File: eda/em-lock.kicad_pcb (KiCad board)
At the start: 2 copper layers, 55.9 x 55.9 mm, 81 parts, among them CON1 BARREL_JACK, P1 EXT_LED_CONN, P10 BOOT_SEL_CONN, P12 SWD_CONN, P2 RC522A, P3 RC522B, P4 BTN_OPEN, P5 BTN_CALL, P6 ESP8266_CONN, P7 LOCK_CONN, P8 PWR_SELECT, P9 PWR_SW_CONN, Q1 MMBT3906, Q2 MMBT3906, Q3 MMBT3906, Q4 Q_NMOS_DGS, SW1 RST_BTN, U1 74LVC2G14, U2 LD1117S33CTR, U3 STM32F103C8Tx, Y1 8MHz

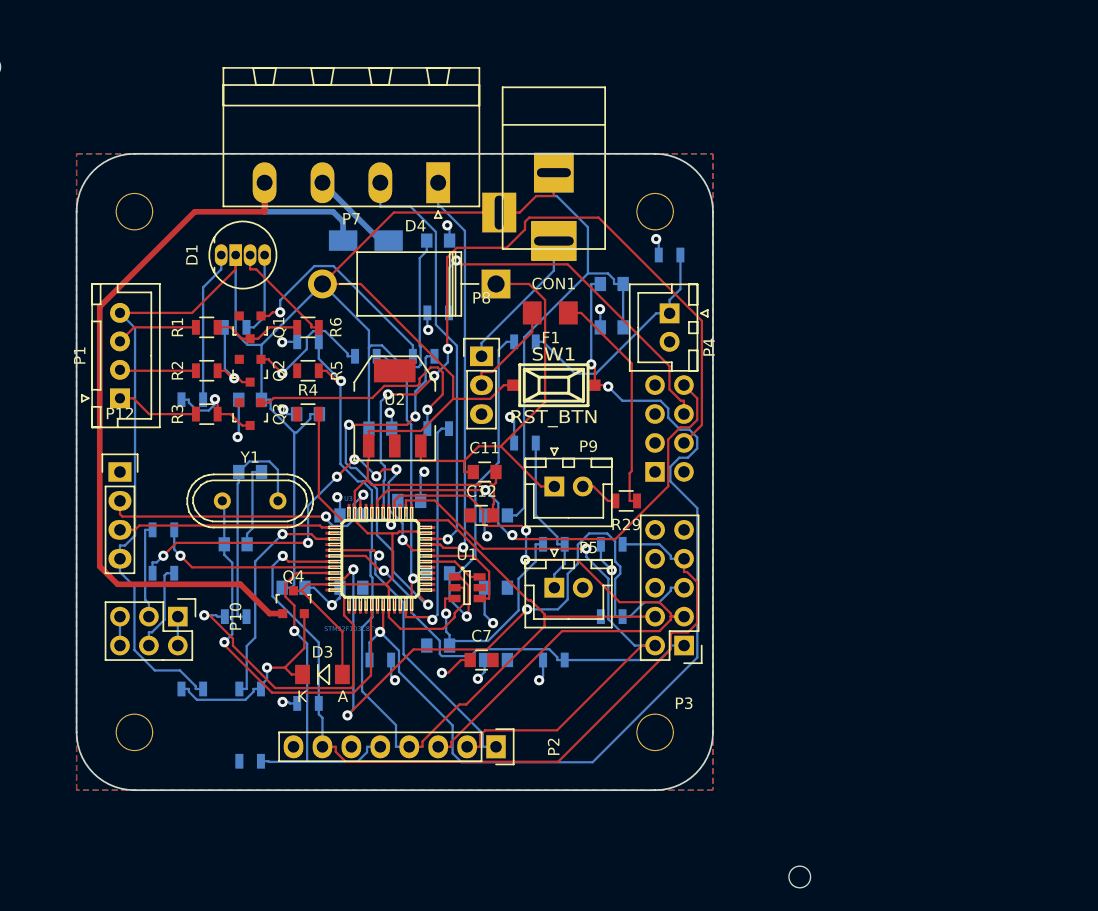
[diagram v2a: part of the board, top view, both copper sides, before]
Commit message: refs #41563 rc522 moved up, RGB LEDs moved to separate pcbs, 3d model of rc522 implemented.
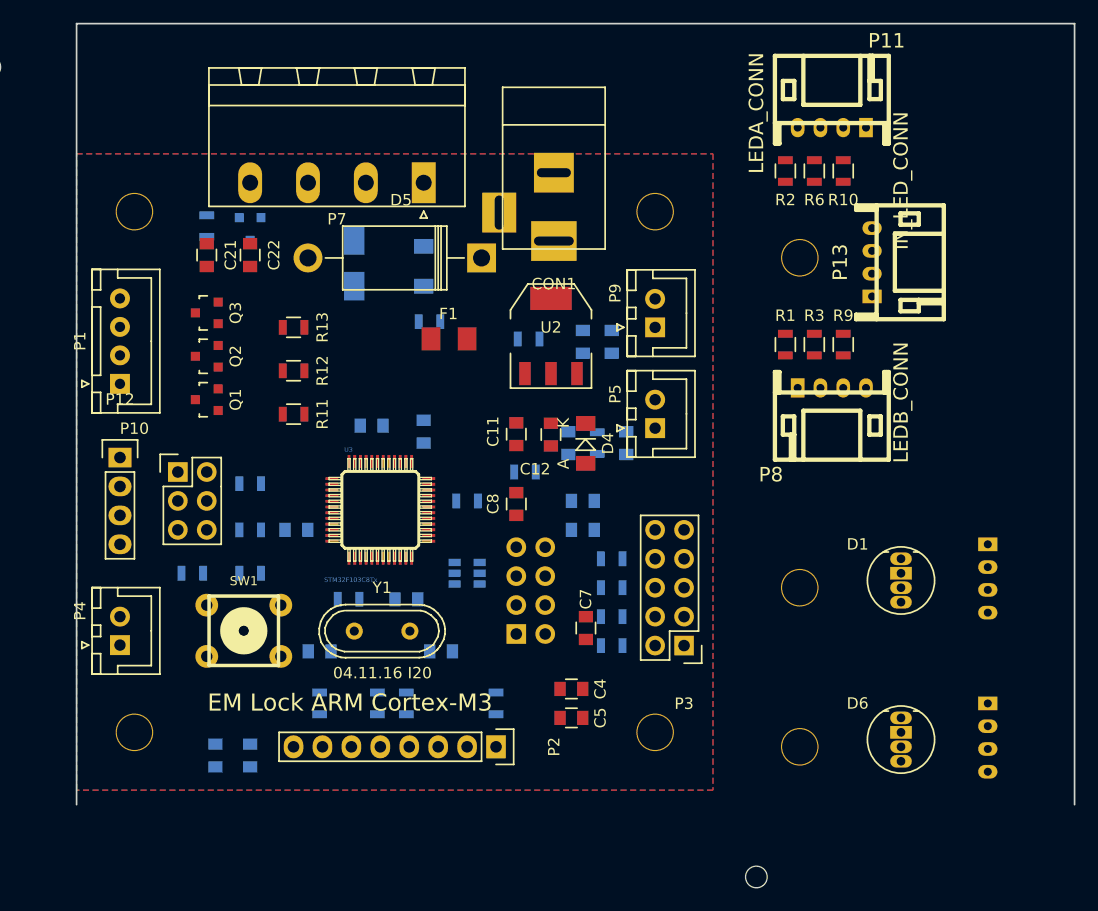
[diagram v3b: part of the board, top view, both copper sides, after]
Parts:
- removed R29: 0, I20:R_0805
- added C21: 10uF, I20:C_0805, F.Cu at (47.0, 95.2)
- added C22: 100nF, I20:C_0805, F.Cu at (50.8, 95.2)
- added D5: 0, I20:Diode_DO-201AD_Horizontal_RM15, F.Cu at (71.1, 95.5)
- added D6: LED_RCBG, I20:LED-RGB-5MM_Common_Cathode, F.Cu at (108.0, 135.9)
- added H3: MountingHole_3.1mm, I20:MountingHole_3.1mm, F.Cu at (99.1, 95.5)
- added H4: MountingHole_3.1mm, I20:MountingHole_3.1mm, F.Cu at (99.1, 138.4)
- added H4: MountingHole_3.1mm, I20:MountingHole_3.1mm, F.Cu at (99.1, 124.5)
- added P11: LEDA_CONN, I20:jst-s4b-ph-kl-angled, F.Cu at (101.9, 84.1)
- added P13: IN_LED_CONN, I20:jst-s4b-ph-kl-angled, F.Cu at (105.4, 95.9)
- added P14: LEDB_CONN, I20:jst-s4b-ph-kl-angled, B.Cu at (115.6, 123.6)
- added P15: LEDB_CONN, I20:jst-s4b-ph-kl-angled, B.Cu at (115.6, 137.6)
- C4, C5, C8, R11, R12, R13: moved to F.Cu
- D3, Q4, R4, R5, U1: moved to B.Cu
- D4: footprint Diodes_ThroughHole:Diode_DO-201AD_Horizontal_RM15 -> I20:MiniMELF_Standard
- P2: footprint Pin_Headers:Pin_Header_Straight_1x08 -> RC522_Full
- P6: footprint ESP8266_CONN -> I20:ESP8266
- P8: value PWR_SELECT -> LEDB_CONN; footprint I20:Pin_Header_Straight_1x03 -> I20:jst-s4b-ph-kl-angled
- R1: value 10R -> 82R
- R10: value 82R -> 10R; moved to F.Cu
- R2: value 15R -> 82R
- R3: value 82R -> 15R
- R6: value 10R -> 15R
- R9: value 15R -> 10R; moved to F.Cu
- SW1: footprint I20:smd_push -> I20:PCB_PUSH
- moved D1 65.4 mm to (108.0, 121.9), turned to 0 degrees
- moved R10 60.6 mm to (102.9, 87.9), turned to 90 degrees
- moved P4 56.4 mm to (39.4, 129.5), turned to 90 degrees
- moved R2 53.8 mm to (97.8, 87.9), turned to 90 degrees
- moved R3 53.7 mm to (100.3, 103.1), turned to 90 degrees
- moved R9 53.4 mm to (102.9, 103.1), turned to 90 degrees
- moved R1 50.8 mm to (97.8, 103.1), turned to 90 degrees
- moved R14 50.4 mm to (45.7, 123.2)
- moved R6 46.5 mm to (100.3, 87.9), turned to 90 degrees
- moved R23 40.7 mm to (47.0, 92.7), turned to 270 degrees
- moved D3 36.9 mm to (66.0, 96.2), turned to 90 degrees
- moved R19 36.0 mm to (82.5, 127.0)
- moved R24 35.9 mm to (66.5, 101.1), turned to 180 degrees
- moved C20 35.3 mm to (82.5, 102.9), turned to 90 degrees
- moved SW1 34.7 mm to (50.2, 128.2), turned to 90 degrees
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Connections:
- D1 pad 2: GND -> Net-(D1-Pad2)
- F1 pad 2: Net-(F1-Pad2) -> /stm32f103c8/12V_EXT
- P1 pad 1: Net-(P1-Pad1) -> OUT_BLUE
- P1 pad 2: Net-(P1-Pad2) -> OUT_GREEN
- P1 pad 3: Net-(P1-Pad3) -> OUT_RED
- P3 pad 10: Net-(P3-Pad10) -> (no net)
- P3 pad 9: Net-(P3-Pad9) -> (no net)
- P6 pad 3: Net-(P6-Pad3) -> (no net)
- P6 pad 5: Net-(P6-Pad5) -> (no net)
- P8 pad 1: /stm32f103c8/12V_EXT -> Net-(P8-Pad1)
- P8 pad 2: Net-(F1-Pad2) -> Net-(P8-Pad2)
- Q1 pad 3: Net-(Q1-Pad3) -> OUT_BLUE
- Q2 pad 3: Net-(Q2-Pad3) -> OUT_GREEN
- Q3 pad 3: Net-(Q3-Pad3) -> OUT_RED
- R1 pad 1: Net-(Q1-Pad3) -> Net-(P8-Pad1)
- R1 pad 2: Net-(P1-Pad3) -> Net-(P13-Pad1)
- R10 pad 1: Net-(Q3-Pad3) -> Net-(P11-Pad3)
- R10 pad 2: Net-(D1-Pad1) -> Net-(P13-Pad3)
- R2 pad 1: Net-(Q2-Pad3) -> Net-(P11-Pad1)
- R2 pad 2: Net-(P1-Pad2) -> Net-(P13-Pad1)
- R3 pad 1: Net-(Q3-Pad3) -> Net-(P8-Pad2)
- R3 pad 2: Net-(P1-Pad1) -> Net-(P13-Pad2)
- R6 pad 1: Net-(Q1-Pad3) -> Net-(P11-Pad2)
- R6 pad 2: Net-(D1-Pad3) -> Net-(P13-Pad2)
- R9 pad 1: Net-(Q2-Pad3) -> Net-(P8-Pad3)
- R9 pad 2: Net-(D1-Pad4) -> Net-(P13-Pad3)
- U3 pad 10: Net-(U3-Pad10) -> (no net)
- U3 pad 14: Net-(U3-Pad14) -> (no net)
- U3 pad 15: Net-(U3-Pad15) -> (no net)
- U3 pad 16: Net-(U3-Pad16) -> (no net)
- U3 pad 17: Net-(U3-Pad17) -> (no net)
- U3 pad 2: Net-(U3-Pad2) -> (no net)
- U3 pad 25: Net-(U3-Pad25) -> (no net)
- U3 pad 3: Net-(U3-Pad3) -> (no net)
- U3 pad 32: Net-(U3-Pad32) -> (no net)
- U3 pad 33: Net-(U3-Pad33) -> (no net)
- U3 pad 38: Net-(U3-Pad38) -> (no net)
- U3 pad 4: Net-(U3-Pad4) -> (no net)
- U3 pad 40: Net-(U3-Pad40) -> (no net)
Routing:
- net GND: track 292.6 -> 0.00 mm
- net PB14_SPI2_MISO: track 87.3 -> 0.00 mm, vias 1 -> 0
- net /stm32f103c8/NRST: track 87.0 -> 0.00 mm, vias 3 -> 0
- net PB7_RC522_RST: track 75.4 -> 0.00 mm, vias 1 -> 0
- net LOCK_GND: track 72.5 -> 0.00 mm
- net ESP_RESET: track 68.5 -> 0.00 mm, vias 4 -> 0
- net PB9_RC522B_IRQ: track 62.2 -> 0.00 mm, vias 3 -> 0
- net PB15_SPI2_MOSI: track 60.0 -> 0.00 mm, vias 2 -> 0
- net PB13_SPI2_SCK: track 51.3 -> 0.00 mm, vias 1 -> 0
- net UART_INT_RX: track 42.5 -> 0.00 mm, vias 2 -> 0
- net VCC: track 40.3 -> 0.00 mm, vias 19 -> 0
- net PB5_RC522A_CS: track 39.1 -> 0.00 mm, vias 1 -> 0
- net /stm32f103c8/PB2/BOOT1: track 38.5 -> 0.00 mm, vias 7 -> 0
- net UART_EXT_RX: track 37.7 -> 0.00 mm, vias 1 -> 0
- net PB6_RC522B_CS: track 37.5 -> 0.00 mm, vias 1 -> 0
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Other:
- board size 55.9 x 55.9 mm -> 87.6 x 68.6 mm
- board text added: "04.11.16 I20"
- board text added: "EM Lock ARM Cortex-M3"

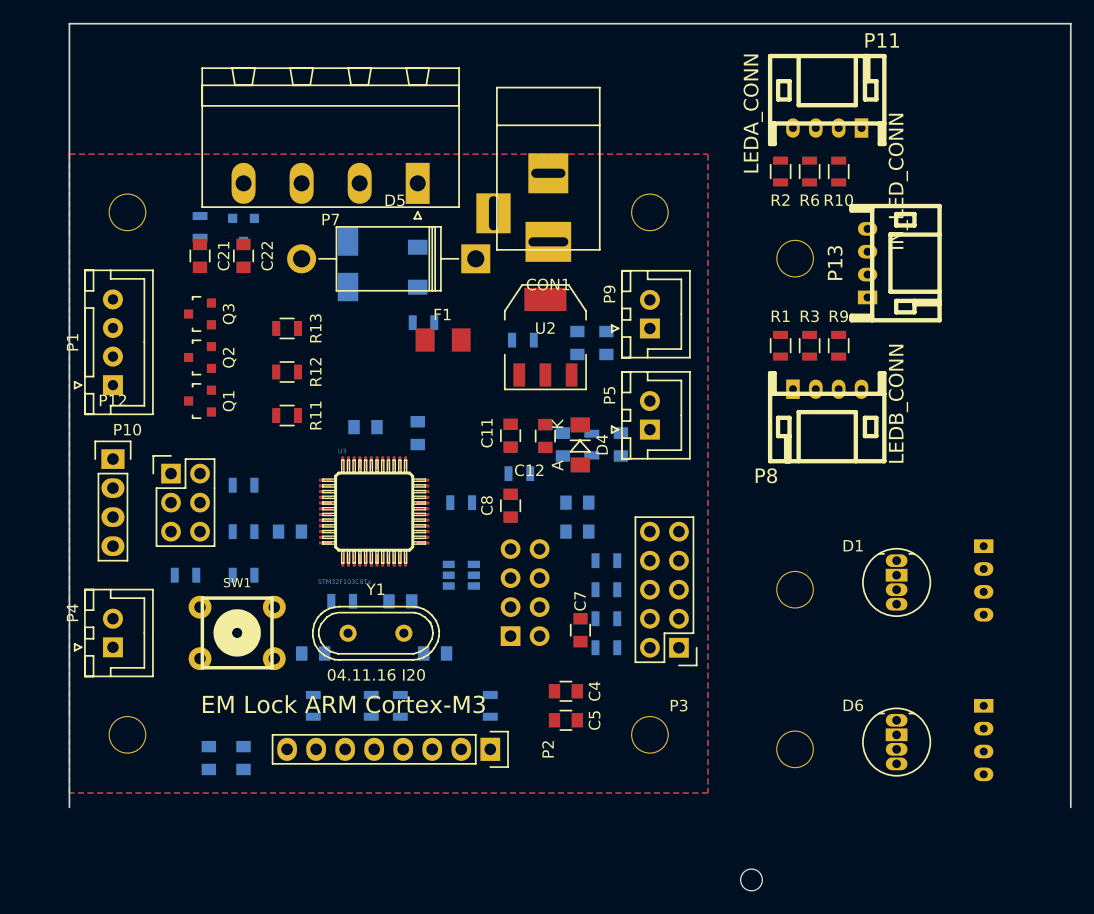
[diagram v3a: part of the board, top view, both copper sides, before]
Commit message: refs #41563 pcb update.
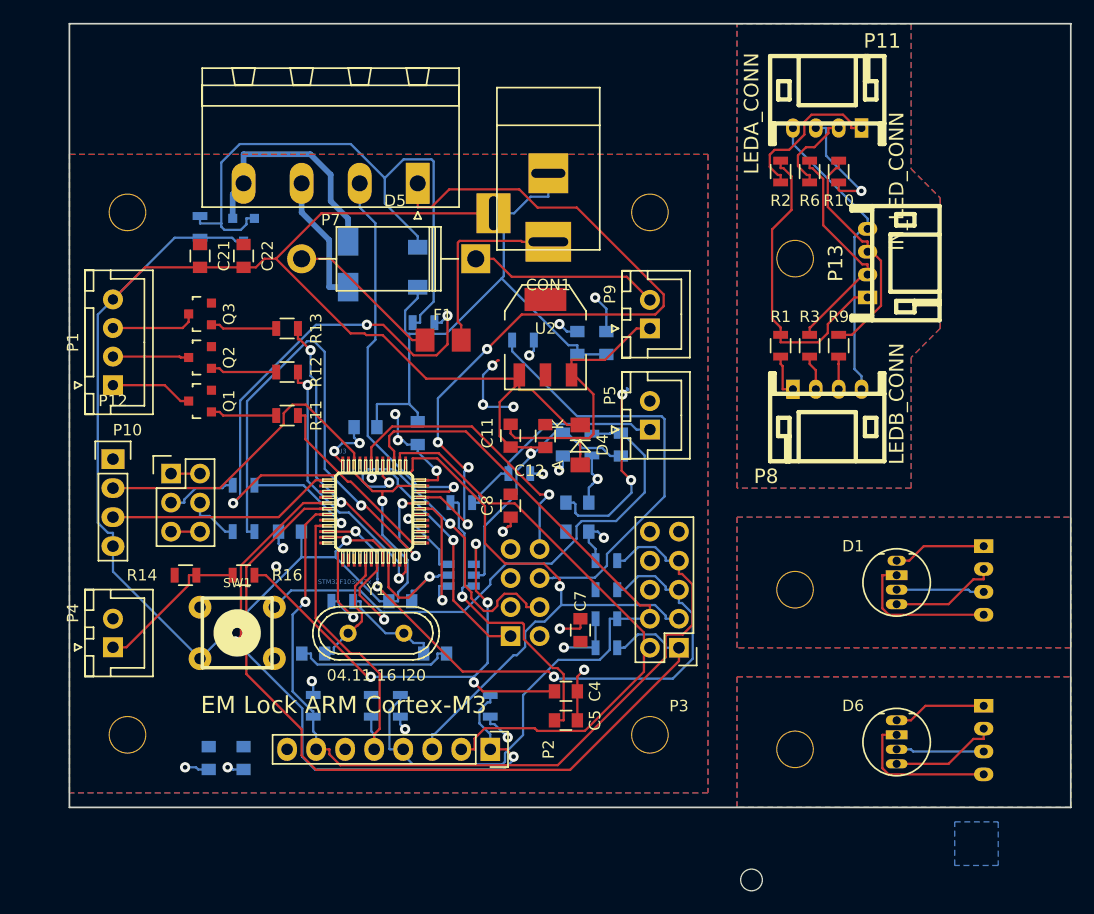
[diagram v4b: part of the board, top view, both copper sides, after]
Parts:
- D6: footprint I20:LED-RGB-5MM_Common_Cathode -> LED-RGB-5MM_Common_Cathode
- P2: footprint RC522_Full -> I20:RC522_Full
- R14, R16: moved to F.Cu
- renumbered H4 to H5, H4 to H6, H3 to H7, H6 to H8, H5 to H9
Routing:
- net GND: track 0.00 -> 258.9 mm, vias 0 -> 3
- net PB7_RC522_RST: track 0.00 -> 75.9 mm, vias 0 -> 1
- net PB6_RC522B_CS: track 0.00 -> 72.7 mm
- net PB14_SPI2_MISO: track 0.00 -> 71.4 mm
- net UART_EXT_TX: track 0.00 -> 69.8 mm, vias 0 -> 4
- net VCC: track 0.00 -> 60.8 mm, vias 0 -> 20
- net PB5_RC522A_CS: track 0.00 -> 56.6 mm, vias 0 -> 2
- net Net-(D3-Pad1): track 0.00 -> 55.6 mm
- net /stm32f103c8/NRST: track 0.00 -> 55.1 mm, vias 0 -> 1
- net PB15_SPI2_MOSI: track 0.00 -> 54.6 mm, vias 0 -> 1
- net PB9_RC522B_IRQ: track 0.00 -> 53.1 mm, vias 0 -> 3
- net PB13_SPI2_SCK: track 0.00 -> 52.2 mm
- net /stm32f103c8/PB2/BOOT1: track 0.00 -> 49.9 mm, vias 0 -> 3
- net LOCK_OPEN: track 0.00 -> 47.8 mm, vias 0 -> 3
- net Net-(C4-Pad2): track 0.00 -> 45.2 mm, vias 0 -> 4
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
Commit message: refs #41563 pcb done (pochti ;))
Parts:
- removed D1: LED_RCBG, I20:LED-RGB-5MM_Common_Cathode
- removed D6: LED_RCBG, LED-RGB-5MM_Common_Cathode
- removed H5, H6, H7: MountingHole_3.1mm, I20:MountingHole_3.1mm
- removed P11: LEDA_CONN, I20:jst-s4b-ph-kl-angled
- removed P13: IN_LED_CONN, I20:jst-s4b-ph-kl-angled
- removed P14, P15, P8: LEDB_CONN, I20:jst-s4b-ph-kl-angled
- removed R1, R2: 82R, I20:R_0805
- removed R10, R9: 10R, I20:R_0805
- removed R3, R6: 15R, I20:R_0805
- CON1: footprint I20:DC-005 -> DC-005
- renumbered SW1 to RESET
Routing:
- net VCC: track 60.8 -> 357.1 mm, vias 20 -> 2
- net GNDD: track 26.3 -> 113.9 mm, vias 5 -> 0
- net PB15_SPI2_MOSI: track 54.6 -> 141.3 mm, vias 1 -> 0
- net PB9_RC522B_IRQ: track 53.1 -> 112.0 mm, vias 3 -> 1
- net PB6_RC522B_CS: track 72.7 -> 110.1 mm, vias 0 -> 1
- net PB14_SPI2_MISO: track 71.4 -> 105.4 mm, vias 0 -> 2
- net Net-(P13-Pad1): track 27.1 -> 0.00 mm
- net Net-(P11-Pad4): track 26.7 -> 0.00 mm
- net UART_EXT_TX: track 69.8 -> 43.3 mm, vias 4 -> 1
- net LOCK_OPEN: track 47.8 -> 23.0 mm, vias 3 -> 1
- net PB5_RC522A_CS: track 56.6 -> 32.6 mm, vias 2 -> 1
- net Net-(D3-Pad1): track 55.6 -> 33.6 mm
- net Net-(P13-Pad3): track 20.6 -> 0.00 mm
- net Net-(P13-Pad2): track 20.3 -> 0.00 mm
- net Net-(P5-Pad1): track 19.6 -> 38.2 mm
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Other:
- board size 87.6 x 68.6 mm -> 55.9 x 55.9 mm
